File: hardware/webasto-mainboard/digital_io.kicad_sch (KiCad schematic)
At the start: 28 parts

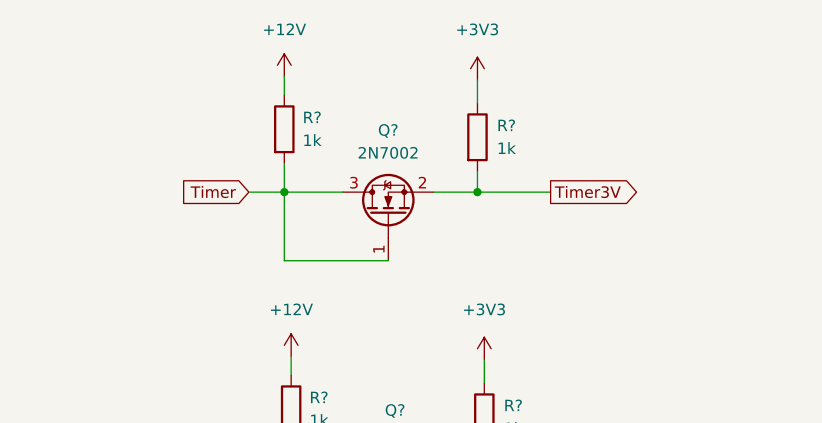
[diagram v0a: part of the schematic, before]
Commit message: Update schematics.  Had a better idea.
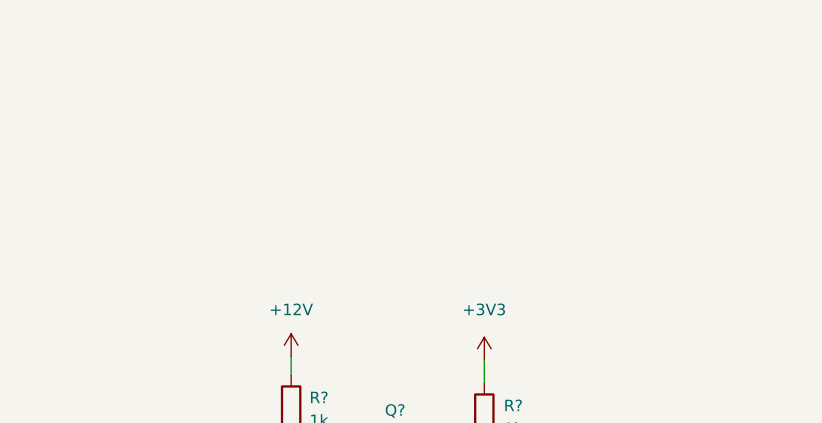
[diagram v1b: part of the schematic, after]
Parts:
- removed Q?: 2N7002, Package_TO_SOT_SMD:SOT-23, symbol Transistor_FET:2N7002
- removed R? (x2): 1k, symbol Device:R
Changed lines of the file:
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@@
   (junction (at 84.074 96.647) (diameter 0) (color 0 0 0 0)
   )
-  (junction (at 62.357 32.512) (diameter 0) (color 0 0 0 0)
-  )
   (junction (at 84.582 63.627) (diameter 0) (color 0 0 0 0)
   )
@@
   (junction (at 217.805 66.04) (diameter 0) (color 0 0 0 0)
   )
-  (junction (at 83.82 32.512) (diameter 0) (color 0 0 0 0)
-  )
   (junction (at 210.566 37.211) (diameter 0) (color 0 0 0 0)
   )
@@
     (stroke (width 0) (type default) (color 0 0 0 0))
   )
-  (wire (pts (xy 62.357 29.337) (xy 62.357 32.512))
-    (stroke (width 0) (type default) (color 0 0 0 0))
-  )
   (wire (pts (xy 210.566 37.211) (xy 210.566 38.354))
     (stroke (width 0) (type default) (color 0 0 0 0))
@@
     (stroke (width 0) (type default) (color 0 0 0 0))
   )
-  (wire (pts (xy 83.82 32.512) (xy 83.82 30.226))
-    (stroke (width 0) (type default) (color 0 0 0 0))
-  )
   (wire (pts (xy 84.582 51.181) (xy 84.582 53.721))
     (stroke (width 0) (type default) (color 0 0 0 0))
@@
     (stroke (width 0) (type default) (color 0 0 0 0))
   )
-  (wire (pts (xy 58.42 32.512) (xy 62.357 32.512))
-    (stroke (width 0) (type default) (color 0 0 0 0))
-  )
   (wire (pts (xy 227.33 75.057) (xy 227.33 76.962))
     (stroke (width 0) (type default) (color 0 0 0 0))
@@
     (stroke (width 0) (type default) (color 0 0 0 0))
   )
-  (wire (pts (xy 62.357 32.512) (xy 68.834 32.512))
-    (stroke (width 0) (type default) (color 0 0 0 0))
-  )
   (wire (pts (xy 62.611 93.472) (xy 62.611 96.647))
     (stroke (width 0) (type default) (color 0 0 0 0))
@@
     (stroke (width 0) (type default) (color 0 0 0 0))
   )
-  (wire (pts (xy 62.357 19.685) (xy 62.357 21.717))
-    (stroke (width 0) (type default) (color 0 0 0 0))
-  )
   (wire (pts (xy 84.836 172.974) (xy 84.836 175.514))
     (stroke (width 0) (type default) (color 0 0 0 0))
@@
     (stroke (width 0) (type default) (color 0 0 0 0))
   )
-  (wire (pts (xy 78.994 32.512) (xy 83.82 32.512))
-    (stroke (width 0) (type default) (color 0 0 0 0))
-  )
-  (wire (pts (xy 83.82 32.512) (xy 91.948 32.512))
-    (stroke (width 0) (type default) (color 0 0 0 0))
-  )
   (wire (pts (xy 63.373 182.245) (xy 63.373 185.42))
     (stroke (width 0) (type default) (color 0 0 0 0))
@@
     (stroke (width 0) (type default) (color 0 0 0 0))
   )
-  (wire (pts (xy 73.914 40.132) (xy 62.357 40.132))
-    (stroke (width 0) (type default) (color 0 0 0 0))
-  )
   (wire (pts (xy 39.624 173.736) (xy 39.624 175.641))
     (stroke (width 0) (type default) (color 0 0 0 0))
@@
     (stroke (width 0) (type default) (color 0 0 0 0))
   )
-  (wire (pts (xy 62.357 40.132) (xy 62.357 32.512))
-    (stroke (width 0) (type default) (color 0 0 0 0))
-  )
   (wire (pts (xy 62.611 96.647) (xy 69.088 96.647))
-    (stroke (width 0) (type default) (color 0 0 0 0))
-  )
-  (wire (pts (xy 83.82 20.066) (xy 83.82 22.606))
     (stroke (width 0) (type default) (color 0 0 0 0))
   )
@@
     )
   )
-  (global_label "Timer3V" (shape output) (at 91.948 32.512 0) (fields_autoplaced)
-    (effects (font (size 1.27 1.27)) (justify left))
-    (property "Intersheet References" "${INTERSHEET_REFS}" (id 0) (at 101.7997 32.4326 0)
-      (effects (font (size 1.27 1.27)) (justify left) hide)
-    )
-  )
   (global_label "KLine" (shape bidirectional) (at 237.871 66.04 0) (fields_autoplaced)
     (effects (font (size 1.27 1.27)) (justify left))
@@
     )
   )
-  (global_label "Timer" (shape input) (at 58.42 32.512 180) (fields_autoplaced)
-    (effects (font (size 1.27 1.27)) (justify right))
-    (property "Intersheet References" "${INTERSHEET_REFS}" (id 0) (at 50.8664 32.4326 0)
-      (effects (font (size 1.27 1.27)) (justify right) hide)
-    )
-  )
   (global_label "CombustionFan3V" (shape input) (at 92.964 185.42 0) (fields_autoplaced)
     (effects (font (size 1.27 1.27)) (justify left))
@@
     (pin "3")
   )
-  (symbol (lib_id "Transistor_FET:2N7002") (at 73.914 35.052 90) (unit 1)
-    (in_bom yes) (on_board yes) (fields_autoplaced)
-    (property "Reference" "Q?" (id 0) (at 73.914 25.654 90))
-    (property "Value" "2N7002" (id 1) (at 73.914 28.194 90))
-    (property "Footprint" "Package_TO_SOT_SMD:SOT-23" (id 2) (at 75.819 29.972 0)
-      (effects (font (size 1.27 1.27) italic) (justify left) hide)
-    )
-    (property "Datasheet" "https://www.onsemi.com/pub/Collateral/NDS7002A-D.PDF" (id 3) (at 73.914 35.052 0)
-      (effects (font (size 1.27 1.27)) (justify left) hide)
-    )
-    (pin "1")
-    (pin "2")
-    (pin "3")
-  )
   (symbol (lib_id "power:GND") (at 158.496 77.724 0) (unit 1)
     (in_bom yes) (on_board yes) (fields_autoplaced)
@@
     )
     (property "Datasheet" "" (id 3) (at 84.836 172.974 0)
-      (effects (font (size 1.27 1.27)) hide)
-    )
-    (pin "1")
-  )
-  (symbol (lib_id "power:+12V") (at 62.357 19.685 0) (unit 1)
-    (in_bom yes) (on_board yes) (fields_autoplaced)
-    (property "Reference" "#PWR?" (id 0) (at 62.357 23.495 0)
-      (effects (font (size 1.27 1.27)) hide)
-    )
-    (property "Value" "+12V" (id 1) (at 62.357 14.478 0))
-    (property "Footprint" "" (id 2) (at 62.357 19.685 0)
-      (effects (font (size 1.27 1.27)) hide)
-    )
-    (property "Datasheet" "" (id 3) (at 62.357 19.685 0)
       (effects (font (size 1.27 1.27)) hide)
     )
@@
     )
     (property "Datasheet" "~" (id 3) (at 227.33 71.247 0)
-      (effects (font (size 1.27 1.27)) hide)
-    )
-    (pin "1")
-    (pin "2")
-  )
-  (symbol (lib_id "Device:R") (at 83.82 26.416 0) (unit 1)
-    (in_bom yes) (on_board yes) (fields_autoplaced)
-    (property "Reference" "R?" (id 0) (at 85.979 25.1459 0)
-      (effects (font (size 1.27 1.27)) (justify left))
-    )
-    (property "Value" "1k" (id 1) (at 85.979 27.6859 0)
-      (effects (font (size 1.27 1.27)) (justify left))
-    )
-    (property "Footprint" "" (id 2) (at 82.042 26.416 90)
-      (effects (font (size 1.27 1.27)) hide)
-    )
-    (property "Datasheet" "~" (id 3) (at 83.82 26.416 0)
       (effects (font (size 1.27 1.27)) hide)
     )
@@
     (pin "3")
   )
-  (symbol (lib_id "Device:R") (at 62.357 25.527 0) (unit 1)
-    (in_bom yes) (on_board yes) (fields_autoplaced)
-    (property "Reference" "R?" (id 0) (at 64.389 24.2569 0)
-      (effects (font (size 1.27 1.27)) (justify left))
-    )
-    (property "Value" "1k" (id 1) (at 64.389 26.7969 0)
-      (effects (font (size 1.27 1.27)) (justify left))
-    )
-    (property "Footprint" "" (id 2) (at 60.579 25.527 90)
-      (effects (font (size 1.27 1.27)) hide)
-    )
-    (property "Datasheet" "~" (id 3) (at 62.357 25.527 0)
-      (effects (font (size 1.27 1.27)) hide)
-    )
-    (pin "1")
-    (pin "2")
-  )
   (symbol (lib_id "power:+12V") (at 62.611 83.82 0) (unit 1)
     (in_bom yes) (on_board yes) (fields_autoplaced)
@@
       (effects (font (size 1.27 1.27)) hide)
     )
-    (pin "1")
-  )
-  (symbol (lib_id "power:+3V3") (at 83.82 20.066 0) (unit 1)
-    (in_bom yes) (on_board yes) (fields_autoplaced)
-    (property "Reference" "#PWR?" (id 0) (at 83.82 23.876 0)
-      (effects (font (size 1.27 1.27)) hide)
-    )
-    (property "Value" "+3V3" (id 1) (at 83.82 14.478 0))
-    (property "Footprint" "" (id 2) (at 83.82 20.066 0)
-      (effects (font (size 1.27 1.27)) hide)
-    )
-    (property "Datasheet" "" (id 3) (at 83.82 20.066 0)
-      (effects (font (size 1.27 1.27)) hide)
-    )

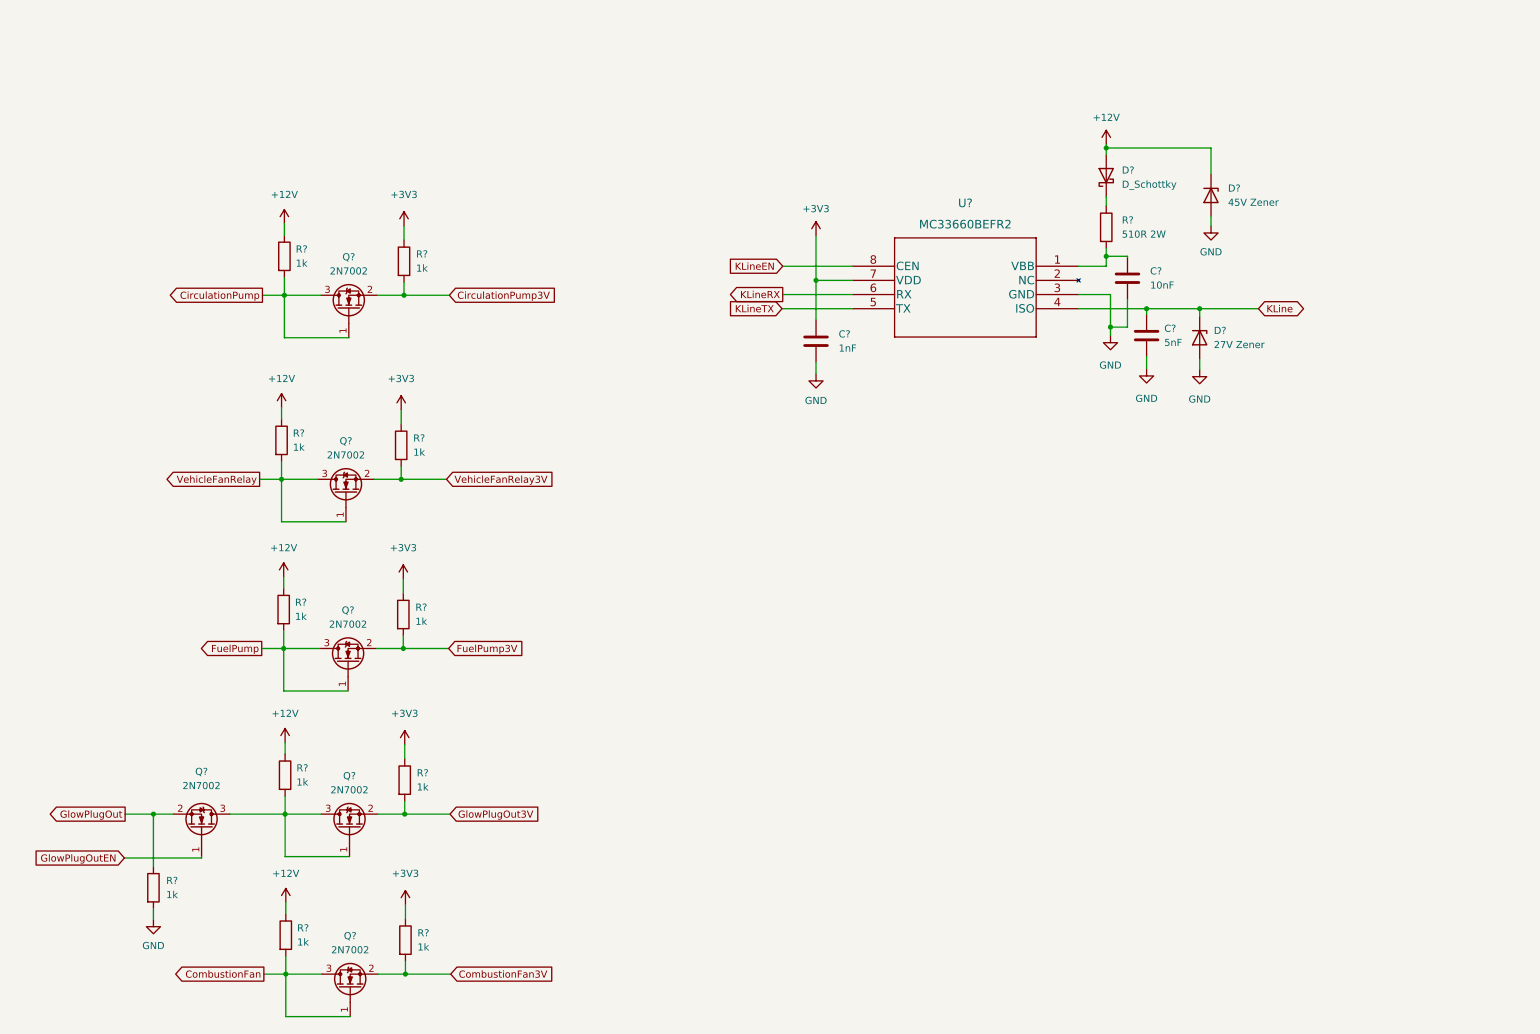
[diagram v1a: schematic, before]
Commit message: More moving of stuff to sensor boards
- not sure I have the glow plug part right quite yet.
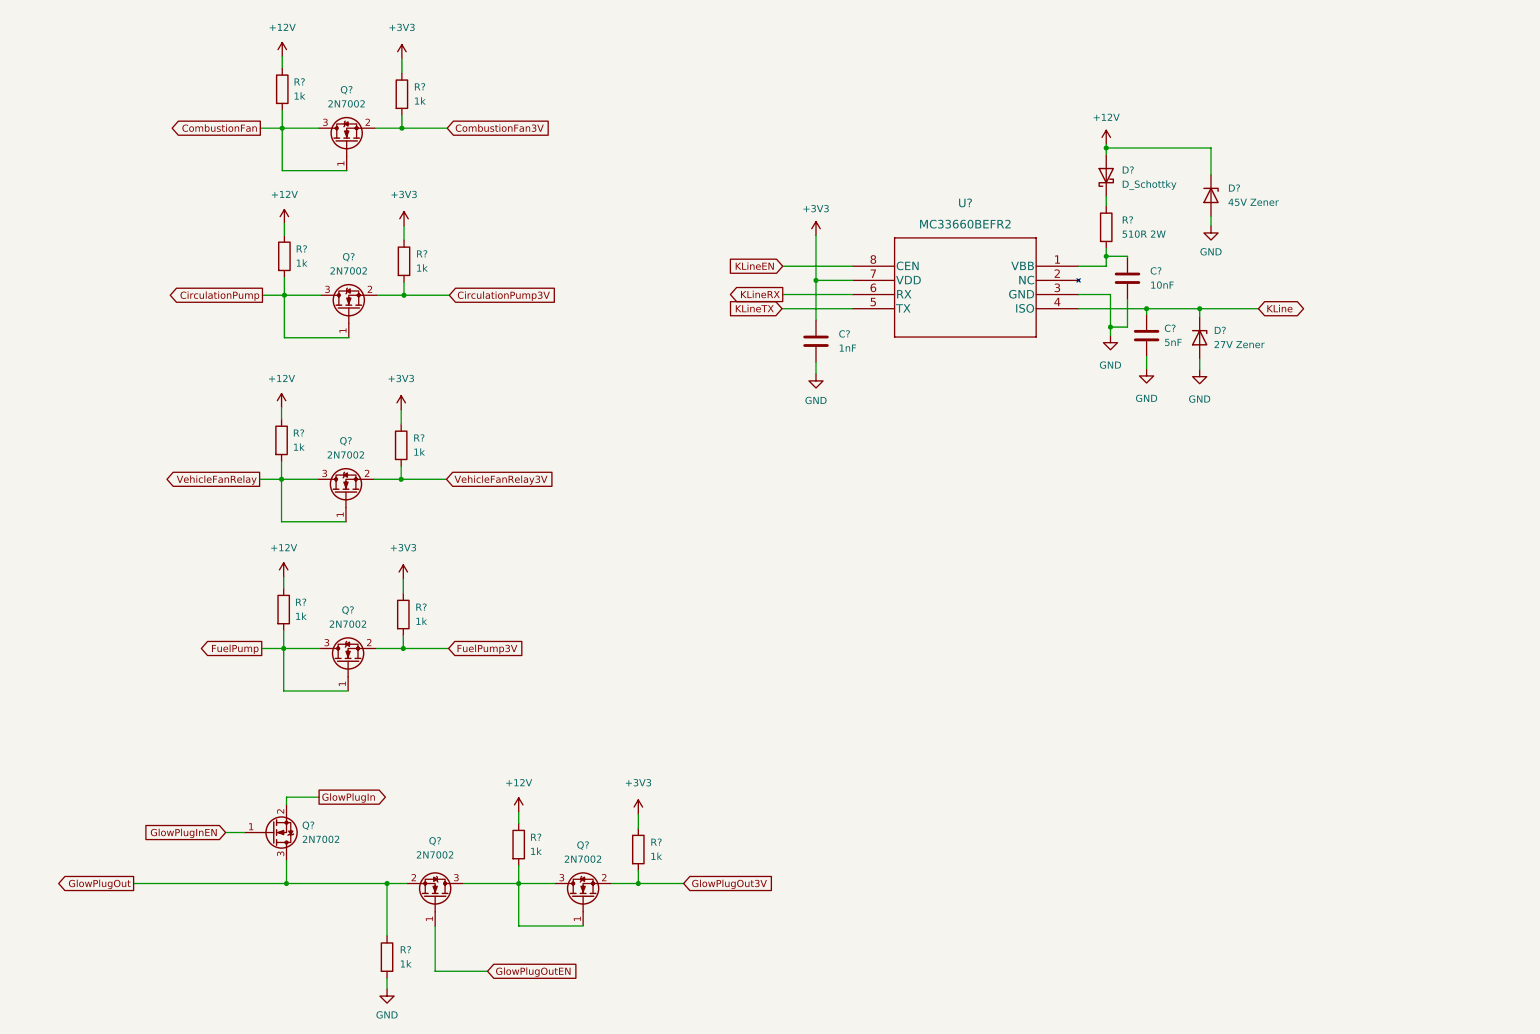
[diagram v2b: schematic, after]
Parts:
- added Q?: 2N7002, Package_TO_SOT_SMD:SOT-23, symbol Transistor_FET:2N7002
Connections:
- net GlowPlugOut: now also Q?.3 (D)
- new net GlowPlugIn: Q?.2 (S)
- new net GlowPlugInEN: Q?.1 (G)
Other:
- moved on the sheet: Q?, R?

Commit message: Added QWIIC Interface schematic, more cleanup
- redid all the MOSFET drives.  The fan one still concerns me a bit.
  is it supposed to DRIVE a relay, or BE a relay?  As long as it's a 12V
  relay, we should be good.
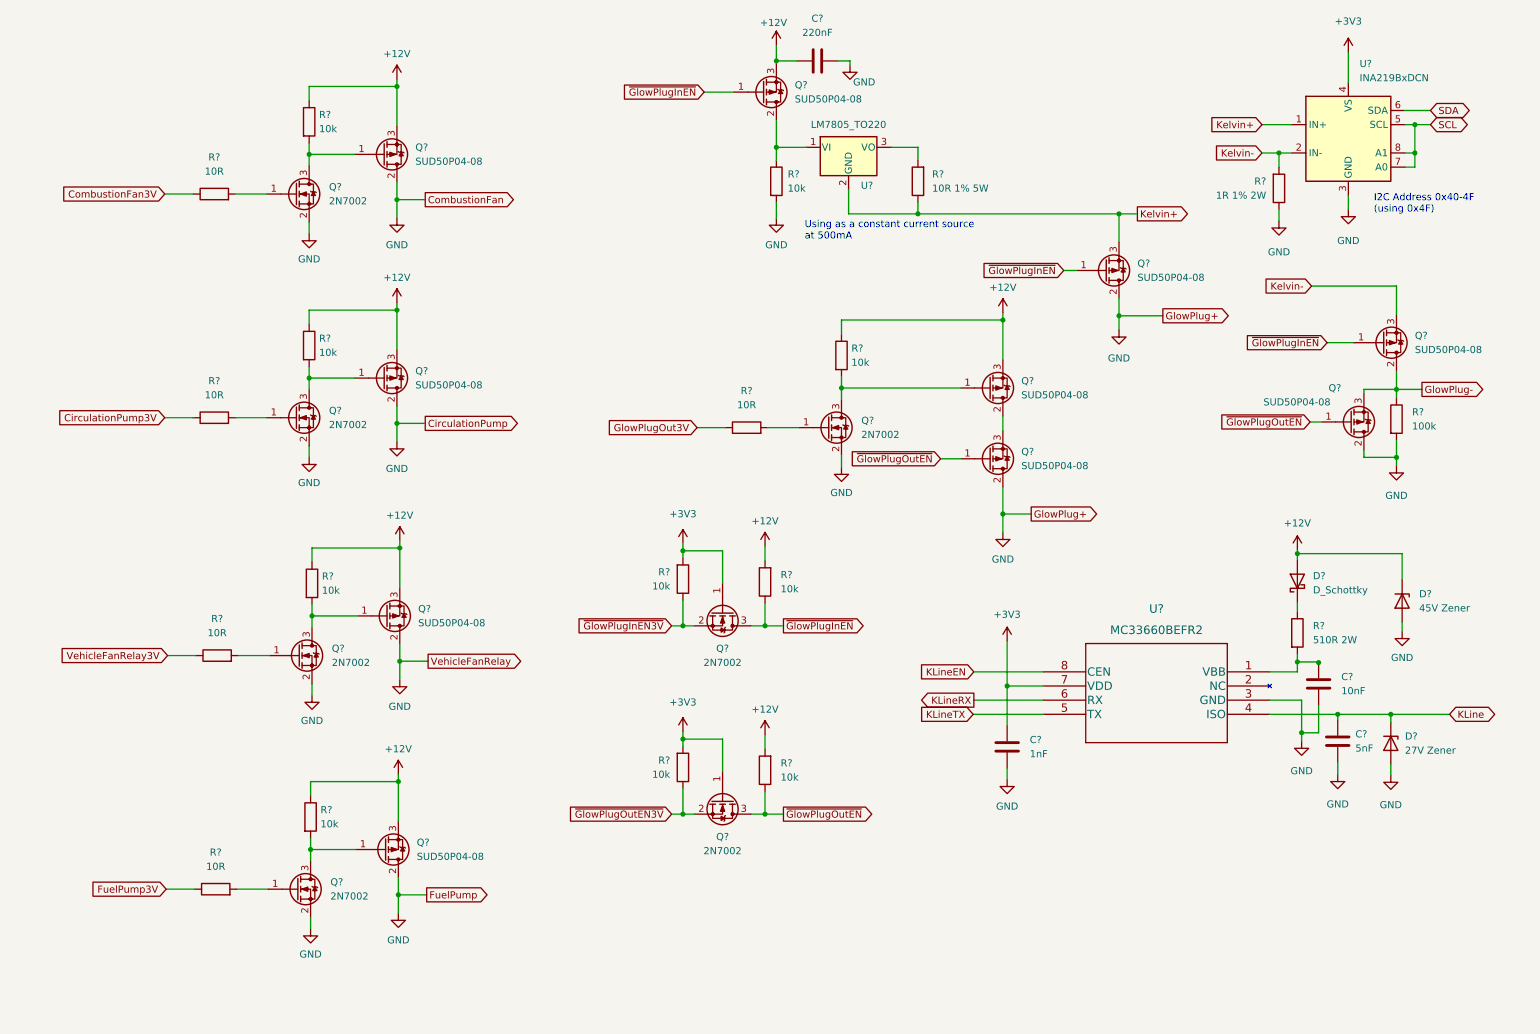
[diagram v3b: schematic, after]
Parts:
- removed Q? (x7): 2N7002, Package_TO_SOT_SMD:SOT-23, symbol Transistor_FET:2N7002
- removed R? (x11): 1k, symbol Device:R
- added C?: 220nF, symbol Device:C
- added Q? (x10): SUD50P04-08, Package_TO_SOT_SMD:TO-252-2, symbol Transistor_FET:SUD50P04-08
- added Q? (x7): 2N7002, Package_TO_SOT_SMD:SOT-23, symbol Transistor_FET:2N7002
- added R? (x10): 10k, symbol Device:R
- added R?: 1R 1% 2W, symbol Device:R
- added R?: 100k, symbol Device:R
- added R? (x5): 10R, symbol Device:R
- added R?: 10R 1% 5W, UltraLibrarian:355010RFT, symbol Device:R
- added U?: LM7805_TO220, Package_TO_SOT_THT:TO-220-3_Vertical, symbol Regulator_Linear:LM7805_TO220
- added U?: INA219BxDCN, Package_TO_SOT_SMD:SOT-23-8, symbol Analog_ADC:INA219BxDCN
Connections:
- net +12V: now also C?.1, Q?.3 (S), Q?.3 (S), Q?.3 (S), Q?.3 (S), Q?.3 (S), Q?.3 (S), R?.1, R?.1, R?.1, R?.1, R?.1, R?.2, R?.2
- net +3V3: now also Q?.1 (G), Q?.1 (G), R?.2, R?.2, U?.4 (VS)
- net CirculationPump3V: now also R?.1
- net CombustionFan3V: now also R?.1
- net FuelPump3V: now also R?.1
- net GND: now also C?.2, Q?.2 (D), Q?.2 (D), Q?.2 (D), Q?.2 (D), Q?.2 (D), Q?.2 (D), Q?.2 (D), Q?.2 (S), Q?.2 (S), Q?.2 (S), Q?.2 (S), Q?.2 (S), R?.1, R?.2, R?.2, U?.3 (GND)
- net GlowPlugOut3V: now also R?.1
- net VehicleFanRelay3V: now also R?.1
- new net: Q?.2 (D), R?.1, U?.1 (VI)
- new net: R?.2, U?.3 (VO)
- new net: Q?.1 (G), R?.2 (x5)
- new net: Q?.1 (G), Q?.3 (D), R?.2 (x5)
- new net: Q?.2 (D), Q?.3 (S)
- new net GlowPlug-: Q?.2 (D), Q?.3 (S), R?.1
- new net Kelvin+: Q?.3 (S), R?.1, U?.1 (IN+), U?.2 (GND)
- new net Kelvin-: Q?.3 (S), R?.2, U?.2 (IN-)
- new net SCL: U?.5 (SCL), U?.7 (A0), U?.8 (A1)
- new net SDA: U?.6 (SDA)
- new net ~{GlowPlugInEN3V}: Q?.2 (S), R?.1
- new net ~{GlowPlugInEN}: Q?.1 (G), Q?.1 (G), Q?.1 (G), Q?.3 (D), R?.1
- new net ~{GlowPlugOutEN3V}: Q?.2 (S), R?.1
- new net ~{GlowPlugOutEN}: Q?.1 (G), Q?.1 (G), Q?.3 (D), R?.1
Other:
- note added: "I2C Address 0x40-4F (using 0x4F)"
- note added: "Using as a constant current source at 500mA"
- moved on the sheet: C?, D?, R?, U?
